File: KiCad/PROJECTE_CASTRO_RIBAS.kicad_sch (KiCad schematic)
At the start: 0 parts

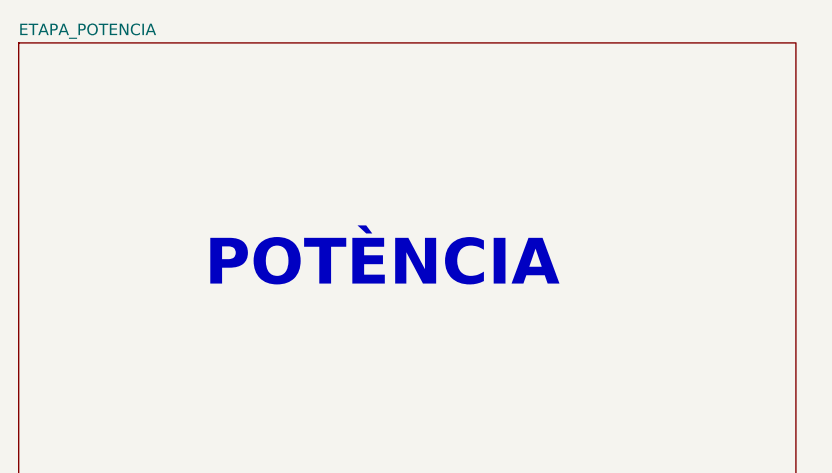
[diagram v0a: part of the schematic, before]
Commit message: Noms dels esquemàtics canviats a Alimentació
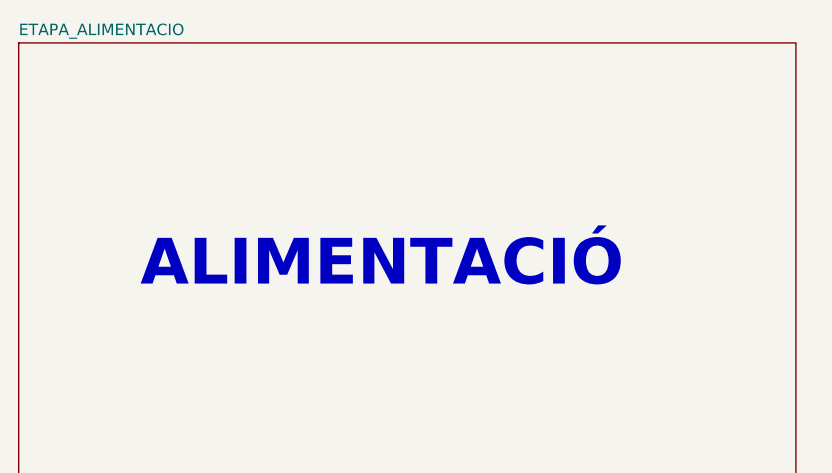
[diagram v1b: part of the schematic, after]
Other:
- sheet ETAPA_POTENCIA renamed ETAPA_ALIMENTACIO
- note added: "ALIMENTACIÓ"
- note removed: "POTÈNCIA"
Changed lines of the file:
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@@
 		)
 	)
-	(text "POTÈNCIA"
+	(text "ALIMENTACIÓ"
 		(exclude_from_sim no)
 		(at 77.216 51.308 0)
@@
 			(color 0 0 0 0.0000)
 		)
-		(property "Sheetname" "ETAPA_POTENCIA"
+		(property "Sheetname" "ETAPA_ALIMENTACIO"
 			(at 36.83 25.9584 0)
 			(effects
